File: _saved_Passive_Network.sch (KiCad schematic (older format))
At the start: 154 parts, among them J18 CONN_01X03, J19 CONN_01X03, J20 CONN_01X08, SW2 SW_Rotary3x4, X1 P7002SCLRP, X2 P7002SCLRP, X3 P7002SCLRP, X4 P7002SCLRP, X5 P7002SCLRP, X6 P7002SCLRP

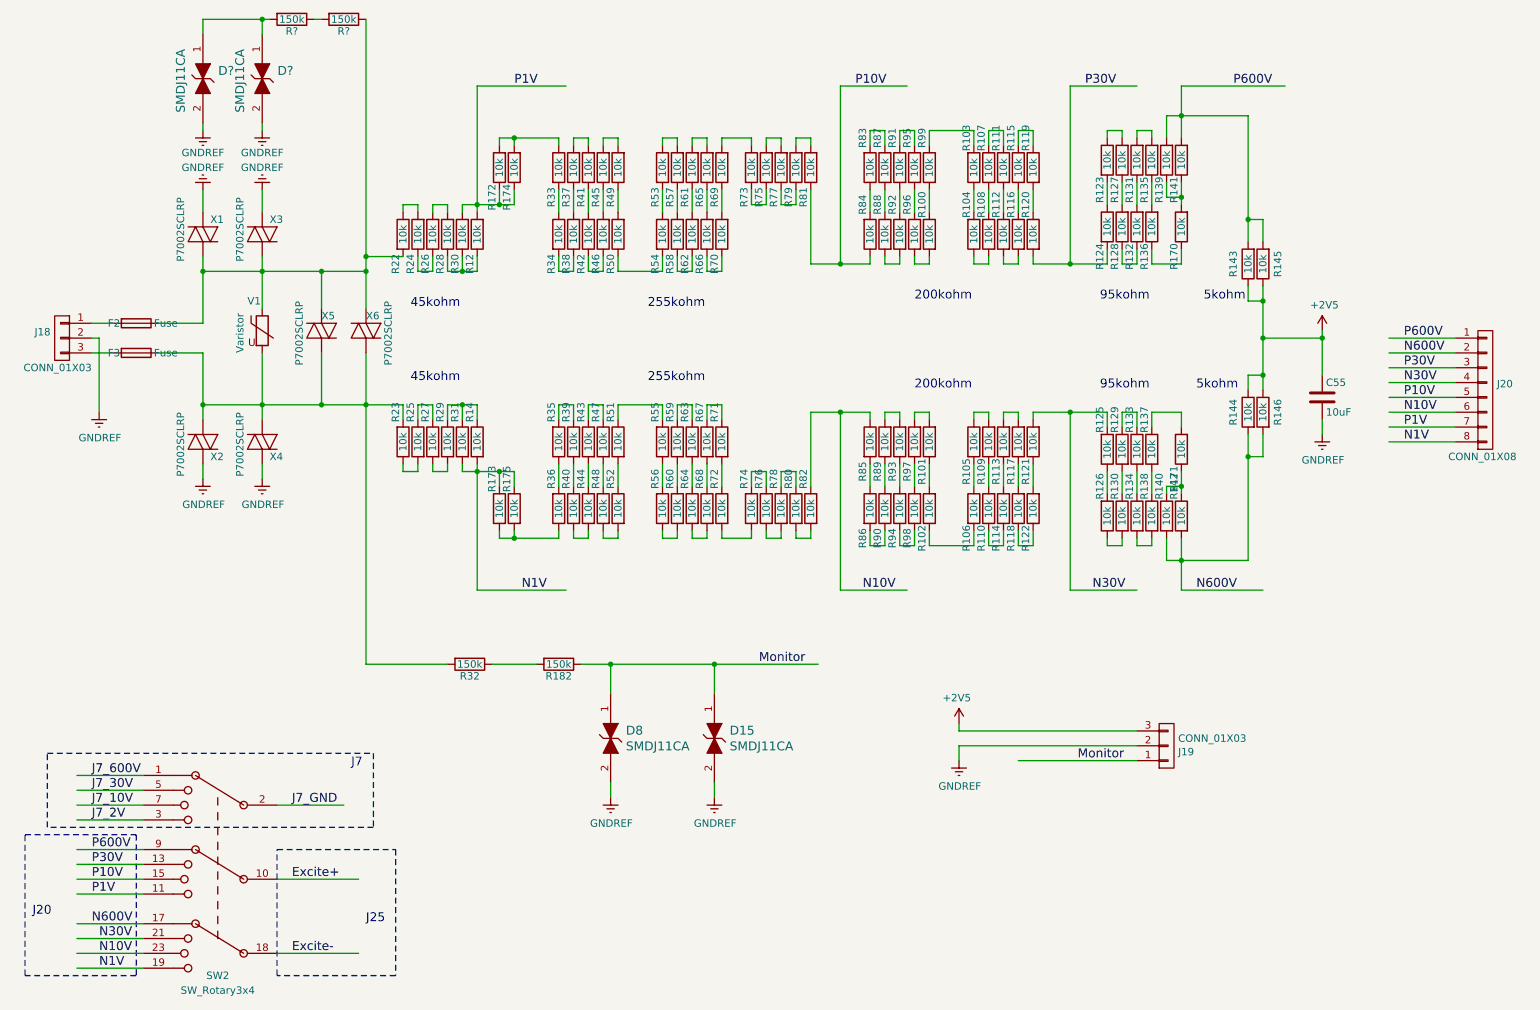
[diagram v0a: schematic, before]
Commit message: Balanced Resistor 추가
D28 D29, R186, R187 추가
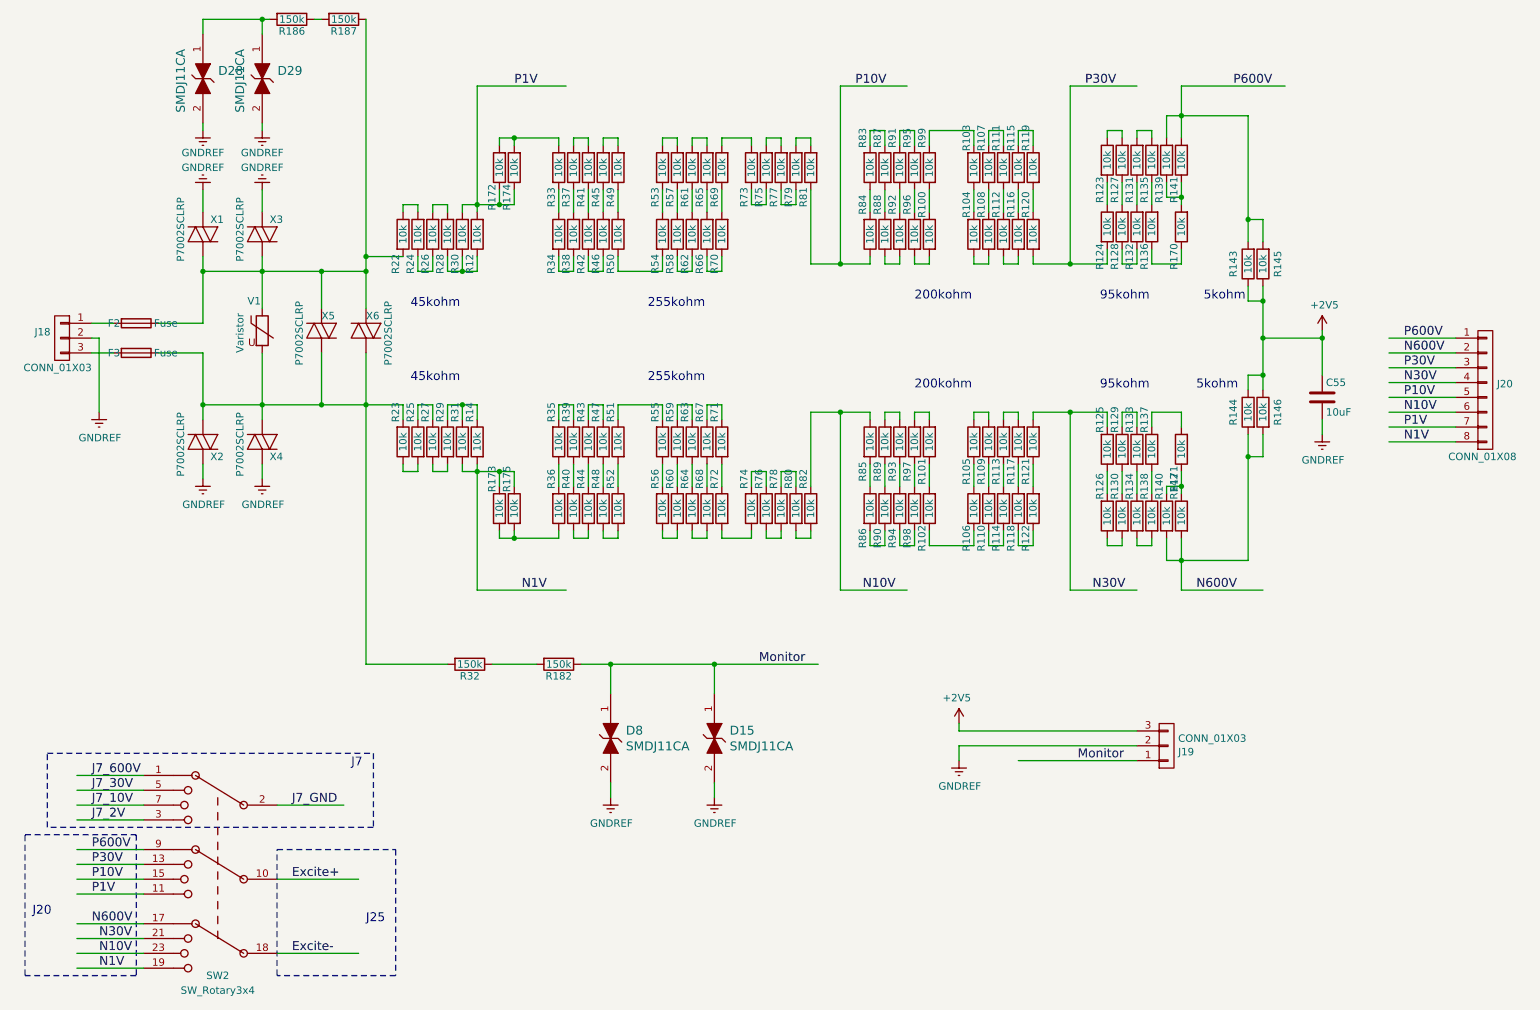
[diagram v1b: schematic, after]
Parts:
- gave numbers to parts that had none: 4
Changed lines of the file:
@@
 	8700 4600 9250 4600
 Wire Wire Line
-	9150 4400 8600 4400
+	8600 4400 9150 4400
 Wire Wire Line
 	8700 4250 8700 4600
 Wire Wire Line
-	9150 3550 9150 4400
+	9150 4400 9150 3550
 Wire Wire Line
 	1250 7050 1700 7050
@@
 Connection ~ 4850 5100
 $Comp
-L GNDREF #PWR?
+L GNDREF #PWR0172
 U 1 1 5B5594BD
 P 2500 1500
-F 0 "#PWR?" H 2500 1250 50  0001 C CNN
+F 0 "#PWR0172" H 2500 1250 50  0001 C CNN
 F 1 "GNDREF" H 2500 1350 50  0000 C CNN
 F 2 "" H 2500 1500 50  0001 C CNN
@@
 $EndComp
 $Comp
-L PGB1010603MR D?
+L PGB1010603MR D29
 U 1 1 5B5594CC
 P 2500 1150
-F 0 "D?" V 2447 1253 60  0000 L CNN
+F 0 "D29" V 2447 1253 60  0000 L CNN
 F 1 "SMDJ11CA" H 2300 1000 60  0000 L CNN
 F 2 "Diodes_SMD:D_SMC_Handsoldering" H 2700 1350 60  0001 L CNN
@@
 $EndComp
 $Comp
-L R R?
+L R R186
 U 1 1 5B5594D3
 P 2700 750
-F 0 "R?" V 2780 750 50  0000 C CNN
+F 0 "R186" V 2780 750 50  0000 C CNN
 F 1 "150k" V 2700 750 50  0000 C CNN
 F 2 "Resistors_THT:R_Axial_Power_L20.0mm_W6.4mm_P22.40mm" V 2630 750 50  0001 C CNN
@@
 	2500 750  2500 850
 $Comp
-L R R?
+L R R187
 U 1 1 5B55E83C
 P 3050 750
-F 0 "R?" V 3130 750 50  0000 C CNN
+F 0 "R187" V 3130 750 50  0000 C CNN
 F 1 "150k" V 3050 750 50  0000 C CNN
 F 2 "Resistors_THT:R_Axial_Power_L20.0mm_W6.4mm_P22.40mm" V 2980 750 50  0001 C CNN
@@
 Connection ~ 2500 750
 $Comp
-L GNDREF #PWR?
+L GNDREF #PWR0171
 U 1 1 5B55F019
 P 2100 1500
-F 0 "#PWR?" H 2100 1250 50  0001 C CNN
+F 0 "#PWR0171" H 2100 1250 50  0001 C CNN
 F 1 "GNDREF" H 2100 1350 50  0000 C CNN
 F 2 "" H 2100 1500 50  0001 C CNN
@@
 $EndComp
 $Comp
-L PGB1010603MR D?
+L PGB1010603MR D28
 U 1 1 5B55F028
 P 2100 1150
-F 0 "D?" V 2047 1253 60  0000 L CNN
+F 0 "D28" V 2047 1253 60  0000 L CNN
 F 1 "SMDJ11CA" H 1900 1000 60  0000 L CNN
 F 2 "Diodes_SMD:D_SMC_Handsoldering" H 2300 1350 60  0001 L CNN
